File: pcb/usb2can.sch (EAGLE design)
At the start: 48 parts, among them CON1 USB_A_MALESMD, IC1 ADM3053M, IC2 LD1117S33

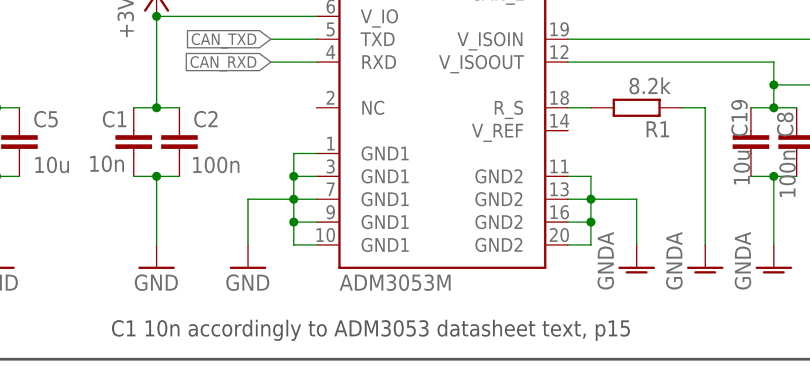
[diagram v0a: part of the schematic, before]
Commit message: Update layout. Make easier to solder
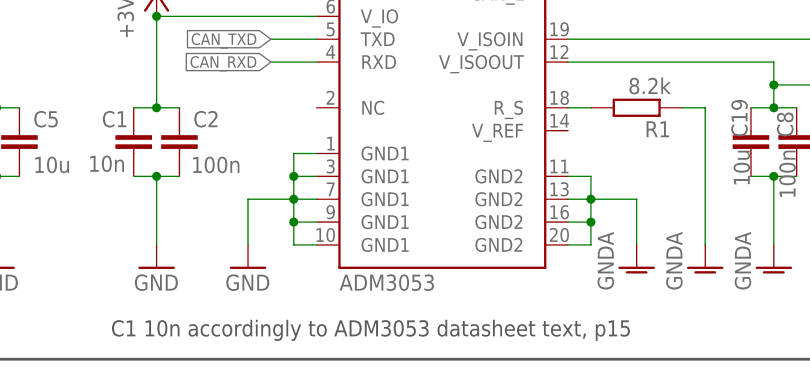
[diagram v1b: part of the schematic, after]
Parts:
- IC1: value ADM3053M -> ADM3053; device ADM3053:ADM3053M -> ADM3053:ADM3053
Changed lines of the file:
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@@
 <?xml version="1.0" encoding="utf-8"?>
 <!DOCTYPE eagle SYSTEM "eagle.dtd">
-<eagle version="6.5.0">
+<eagle version="6.6.0">
 <drawing>
 <settings>
@@
 </classes>
 <parts>
-<part name="IC1" library="ADM3053" deviceset="ADM3053" device="M"/>
+<part name="IC1" library="ADM3053" deviceset="ADM3053" device="" value="ADM3053"/>
 <part name="GND1" library="supply1" deviceset="GND" device=""/>
 <part name="P+1" library="supply1" deviceset="VCC" device=""/>
